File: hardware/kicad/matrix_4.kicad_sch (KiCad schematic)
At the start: 137 parts, among them U12 IS31FL3741A

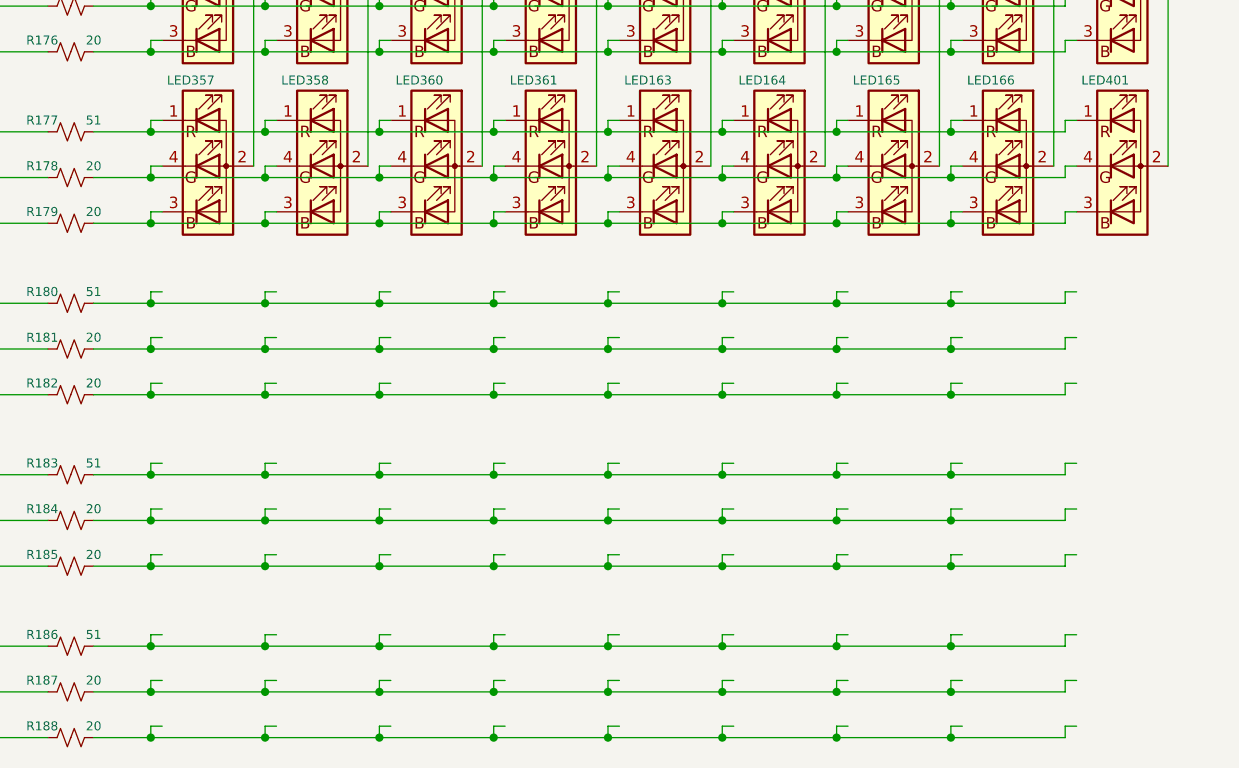
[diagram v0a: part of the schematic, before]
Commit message: route matrices 1,2,4
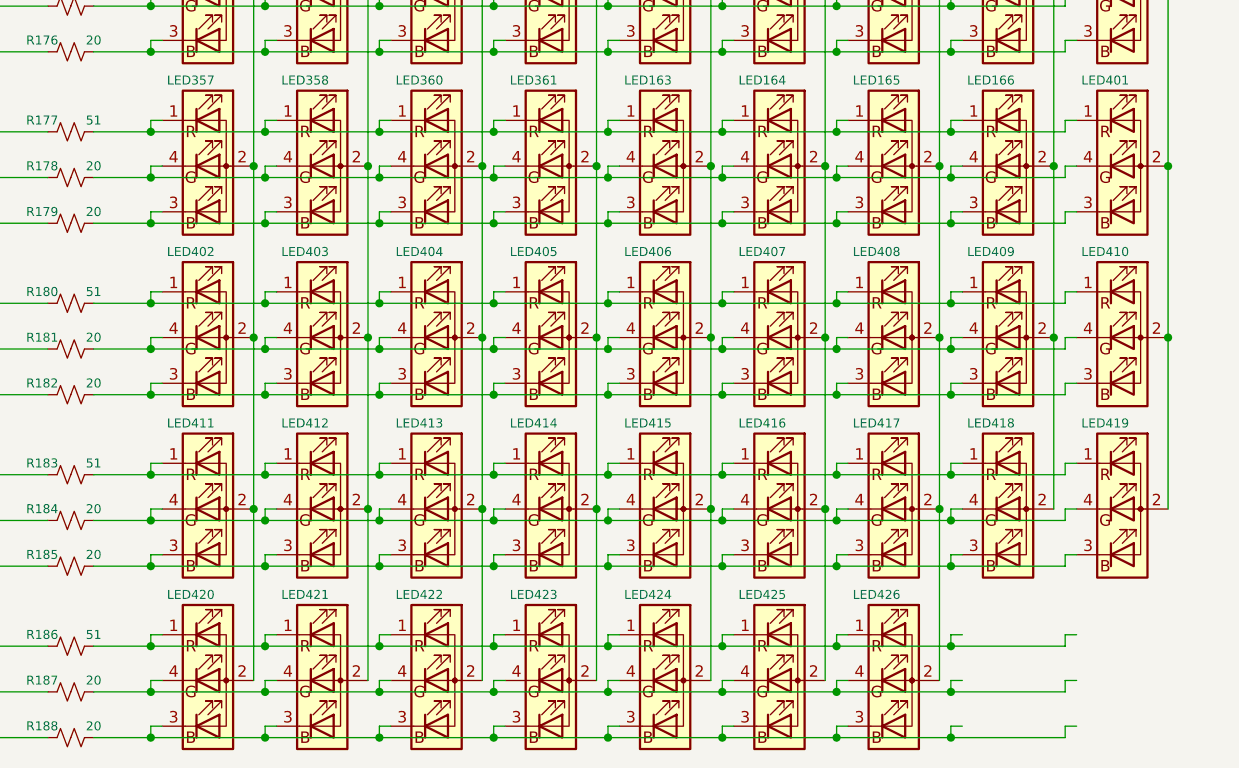
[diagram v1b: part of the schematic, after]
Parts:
- added LED402, LED403, LED404, LED405, LED406, LED407, LED408, LED409, LED410, LED411, LED412, LED413, LED414, LED415, LED416, LED417, LED418, LED419, LED420, LED421, LED422, LED423, LED424, LED425, LED426: LED_ARGB, map_lbr:LED_RGB_0606, symbol Device:LED_RABG
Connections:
- net COL0: now also LED402.2 (A), LED411.2 (A), LED420.2 (A)
- net COL1: now also LED403.2 (A), LED412.2 (A), LED421.2 (A)
- net COL2: now also LED404.2 (A), LED413.2 (A), LED422.2 (A)
- net COL3: now also LED405.2 (A), LED414.2 (A), LED423.2 (A)
- net COL4: now also LED406.2 (A), LED415.2 (A), LED424.2 (A)
- net COL5: now also LED407.2 (A), LED416.2 (A), LED425.2 (A)
- net COL6: now also LED408.2 (A), LED417.2 (A), LED426.2 (A)
- net COL7: now also LED409.2 (A), LED418.2 (A)
- net COL8: now also LED410.2 (A), LED419.2 (A)
- net at R184.2: now also LED411.4 (GK), LED412.4 (GK), LED413.4 (GK), LED414.4 (GK), LED415.4 (GK), LED416.4 (GK), LED417.4 (GK), LED418.4 (GK), LED419.4 (GK)
- net at R186.2: now also LED420.1 (RK), LED421.1 (RK), LED422.1 (RK), LED423.1 (RK), LED424.1 (RK), LED425.1 (RK), LED426.1 (RK)
- net at R188.2: now also LED420.3 (BK), LED421.3 (BK), LED422.3 (BK), LED423.3 (BK), LED424.3 (BK), LED425.3 (BK), LED426.3 (BK)
- net at R182.2: now also LED402.3 (BK), LED403.3 (BK), LED404.3 (BK), LED405.3 (BK), LED406.3 (BK), LED407.3 (BK), LED408.3 (BK), LED409.3 (BK), LED410.3 (BK)
- net at R183.2: now also LED411.1 (RK), LED412.1 (RK), LED413.1 (RK), LED414.1 (RK), LED415.1 (RK), LED416.1 (RK), LED417.1 (RK), LED418.1 (RK), LED419.1 (RK)
- net at R180.2: now also LED402.1 (RK), LED403.1 (RK), LED404.1 (RK), LED405.1 (RK), LED406.1 (RK), LED407.1 (RK), LED408.1 (RK), LED409.1 (RK), LED410.1 (RK)
- net at R187.2: now also LED420.4 (GK), LED421.4 (GK), LED422.4 (GK), LED423.4 (GK), LED424.4 (GK), LED425.4 (GK), LED426.4 (GK)
- net at R181.2: now also LED402.4 (GK), LED403.4 (GK), LED404.4 (GK), LED405.4 (GK), LED406.4 (GK), LED407.4 (GK), LED408.4 (GK), LED409.4 (GK), LED410.4 (GK)
- net at R185.2: now also LED411.3 (BK), LED412.3 (BK), LED413.3 (BK), LED414.3 (BK), LED415.3 (BK), LED416.3 (BK), LED417.3 (BK), LED418.3 (BK), LED419.3 (BK)

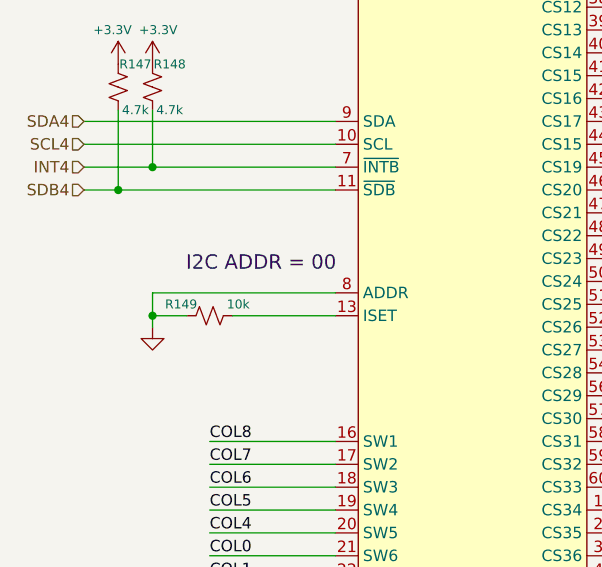
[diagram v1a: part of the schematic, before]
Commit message: update matrix 4 i2c address
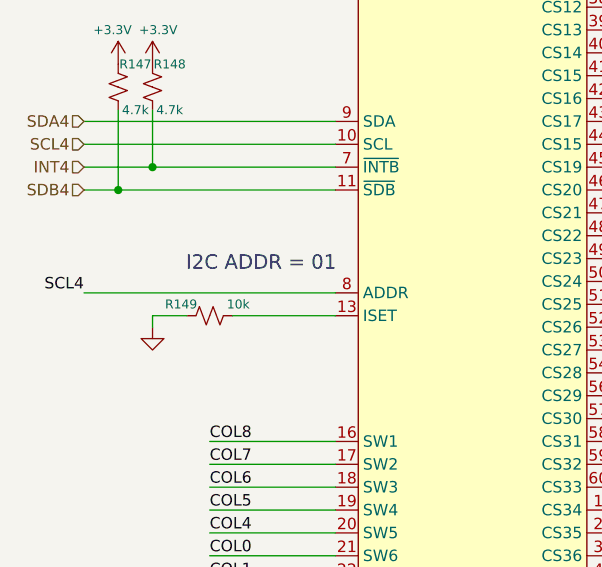
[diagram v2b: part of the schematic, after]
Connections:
- net GND: no longer U12.8 (ADDR)
- net SCL4: now also U12.8 (ADDR)
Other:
- note added: "I2C ADDR = 01"
- note removed: "I2C ADDR = 00"
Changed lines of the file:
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@@
 	)
 	(junction
-		(at 40.64 102.87)
-		(diameter 0)
-		(color 0 0 0 0)
-	)
-	(junction
 		(at 234.95 224.79)
 		(diameter 0)
@@
 	(wire
 		(pts
+			(xy 33.02 100.33) (xy 60.96 100.33)
+		)
+		(stroke
+			(width 0)
+			(type default)
+		)
+	)
+	(wire
+		(pts
 			(xy 158.75 128.27) (xy 160.02 128.27)
 		)
@@
 	(wire
 		(pts
-			(xy 40.64 100.33) (xy 40.64 102.87)
-		)
-		(stroke
-			(width 0)
-			(type default)
-		)
-	)
-	(wire
-		(pts
 			(xy 247.65 91.44) (xy 247.65 90.17)
 		)
@@
 	(wire
 		(pts
-			(xy 40.64 100.33) (xy 60.96 100.33)
-		)
-		(stroke
-			(width 0)
-			(type default)
-		)
-	)
-	(wire
-		(pts
 			(xy 157.48 152.4) (xy 157.48 171.45)
 		)
@@
 		)
 	)
-	(text "I2C ADDR = 00\n"
+	(text "I2C ADDR = 01"
 		(exclude_from_sim no)
 		(at 52.705 97.155 0)
@@
 		(fields_autoplaced yes)
 		(effects
+			(font
+				(size 1.27 1.27)
+			)
+			(justify right bottom)
+		)
+	)
+	(label "SCL4"
+		(at 33.02 100.33 180)
+		(fields_autoplaced yes)
+		(effects

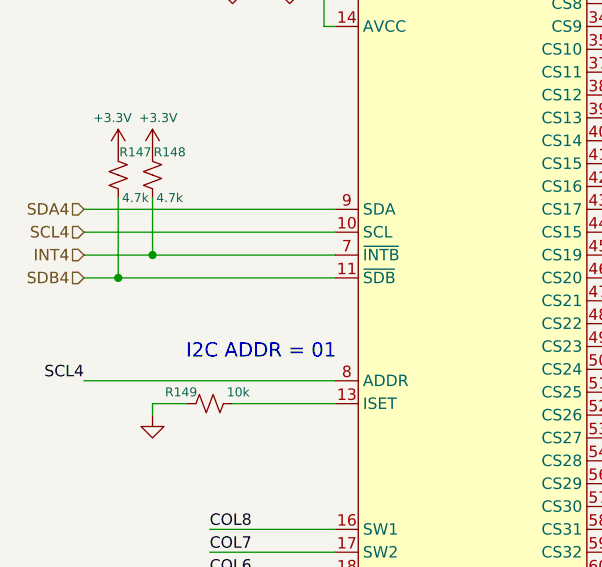
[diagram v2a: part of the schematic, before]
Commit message: esp32c3 upgrade, route usb, fix errors
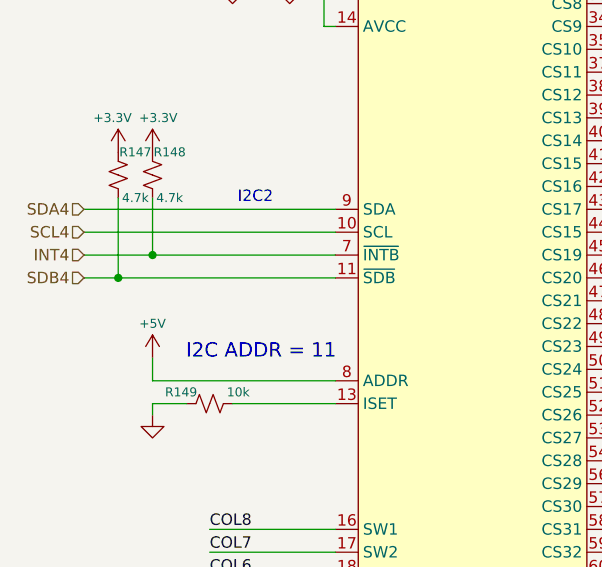
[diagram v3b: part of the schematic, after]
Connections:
- net +5V: now also U12.8 (ADDR)
- net SCL4: no longer U12.8 (ADDR)
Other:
- note added: "I2C ADDR = 11"
- note added: "I2C2"
- note removed: "I2C ADDR = 01"
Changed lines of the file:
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@@
 	(wire
 		(pts
+			(xy 40.64 100.33) (xy 40.64 97.79)
+		)
+		(stroke
+			(width 0)
+			(type default)
+		)
+	)
+	(wire
+		(pts
 			(xy 234.95 229.87) (xy 247.65 229.87)
 		)
@@
 	(wire
 		(pts
+			(xy 60.96 100.33) (xy 40.64 100.33)
+		)
+		(stroke
+			(width 0)
+			(type default)
+		)
+	)
+	(wire
+		(pts
 			(xy 259.08 95.25) (xy 259.08 114.3)
 		)
@@
 	(wire
 		(pts
-			(xy 33.02 100.33) (xy 60.96 100.33)
-		)
-		(stroke
-			(width 0)
-			(type default)
-		)
-	)
-	(wire
-		(pts
 			(xy 158.75 128.27) (xy 160.02 128.27)
 		)
@@
 		)
 	)
-	(text "I2C ADDR = 01"
+	(text "I2C2"
+		(exclude_from_sim no)
+		(at 52.07 80.01 0)
+		(effects
+			(font
+				(size 1.27 1.27)
+			)
+		)
+	)
+	(text "I2C ADDR = 11"
 		(exclude_from_sim no)
 		(at 52.705 97.155 0)
@@
 		)
 	)
-	(label "SCL4"
-		(at 33.02 100.33 180)
-		(fields_autoplaced yes)
-		(effects
-			(font
-				(size 1.27 1.27)
-			)
-			(justify right bottom)
-		)
-	)
 	(label "ROW17"
 		(at 120.65 139.7 0)
@@
 					(unit 1)
 				)
+			)
+		)
+	)
+	(symbol
+		(lib_id "power:+5V")
+		(at 40.64 97.79 0)
+		(unit 1)
+		(exclude_from_sim no)
+		(in_bom yes)
+		(on_board yes)
+		(dnp no)
+		(property "Reference" "#PWR082"
+			(at 40.64 101.6 0)
+			(effects
+				(font
+					(size 1.27 1.27)
+				)
+				(hide yes)
+			)
+		)
+		(property "Value" "+5V"
+			(at 40.64 93.98 0)
+			(effects
+				(font
+					(size 1 1)
+				)
+			)
+		)
+		(property "Footprint" ""
+			(at 40.64 97.79 0)
+			(effects
+				(font
+					(size 1.27 1.27)
+				)
+				(hide yes)
+			)
+		)
+		(property "Datasheet" ""
+			(at 40.64 97.79 0)
+			(effects
+				(font
+					(size 1.27 1.27)
+				)
+				(hide yes)
+			)
+		)
+		(property "Description" "Power symbol creates a global label with name \"+5V\""
+			(at 40.64 97.79 0)
+			(effects
+				(font
+					(size 1.27 1.27)
+				)
+				(hide yes)
+			)
+		)
+		(pin "1"
+		)
+		(instances
+			(project "traffic_paradise"
+				(path "/911505fc-874d-4338-908e-12054bdd5112/229965e3-107a-47b9-9b24-fdc53810a62f"
+					(reference "#PWR082")
+					(unit 1)
+				)
